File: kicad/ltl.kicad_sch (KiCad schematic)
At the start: 59 parts, among them J1 Conn_01x06, Q1 RUM001L02T2CL, Q2 RZM001P02T2L, Q3 BC327, U1 TPL5111, U2 ESP-12E, U3 DS18B20, U4 TPS73733DCQR

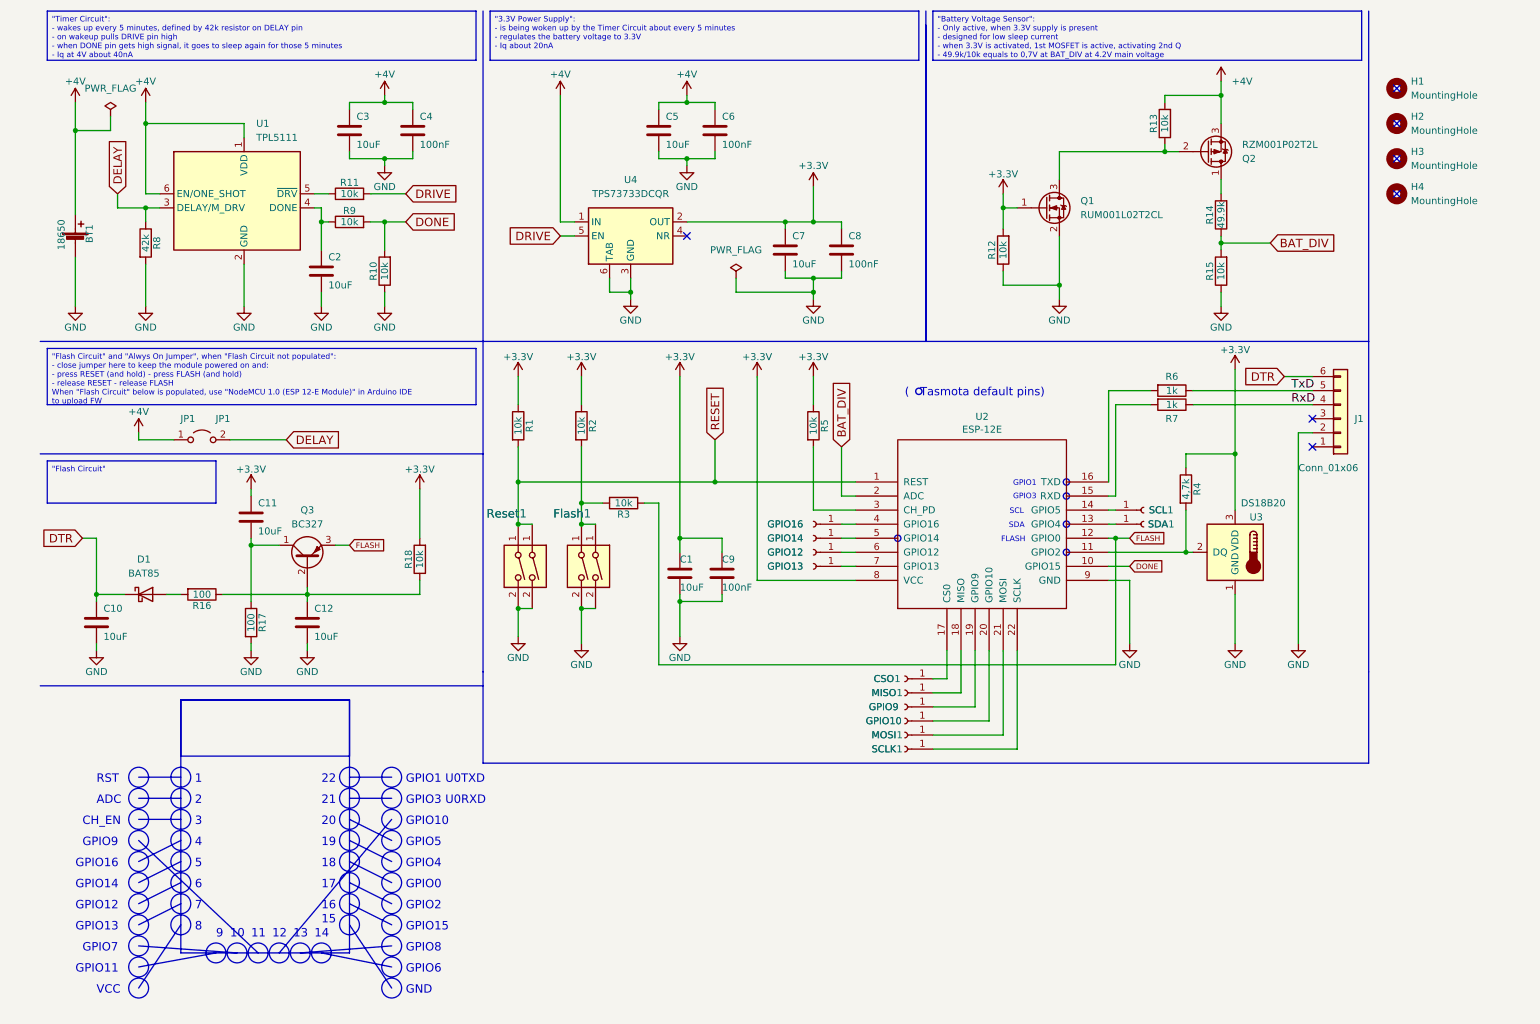
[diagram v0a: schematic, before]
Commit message: Updated PCB to Revision 2.2
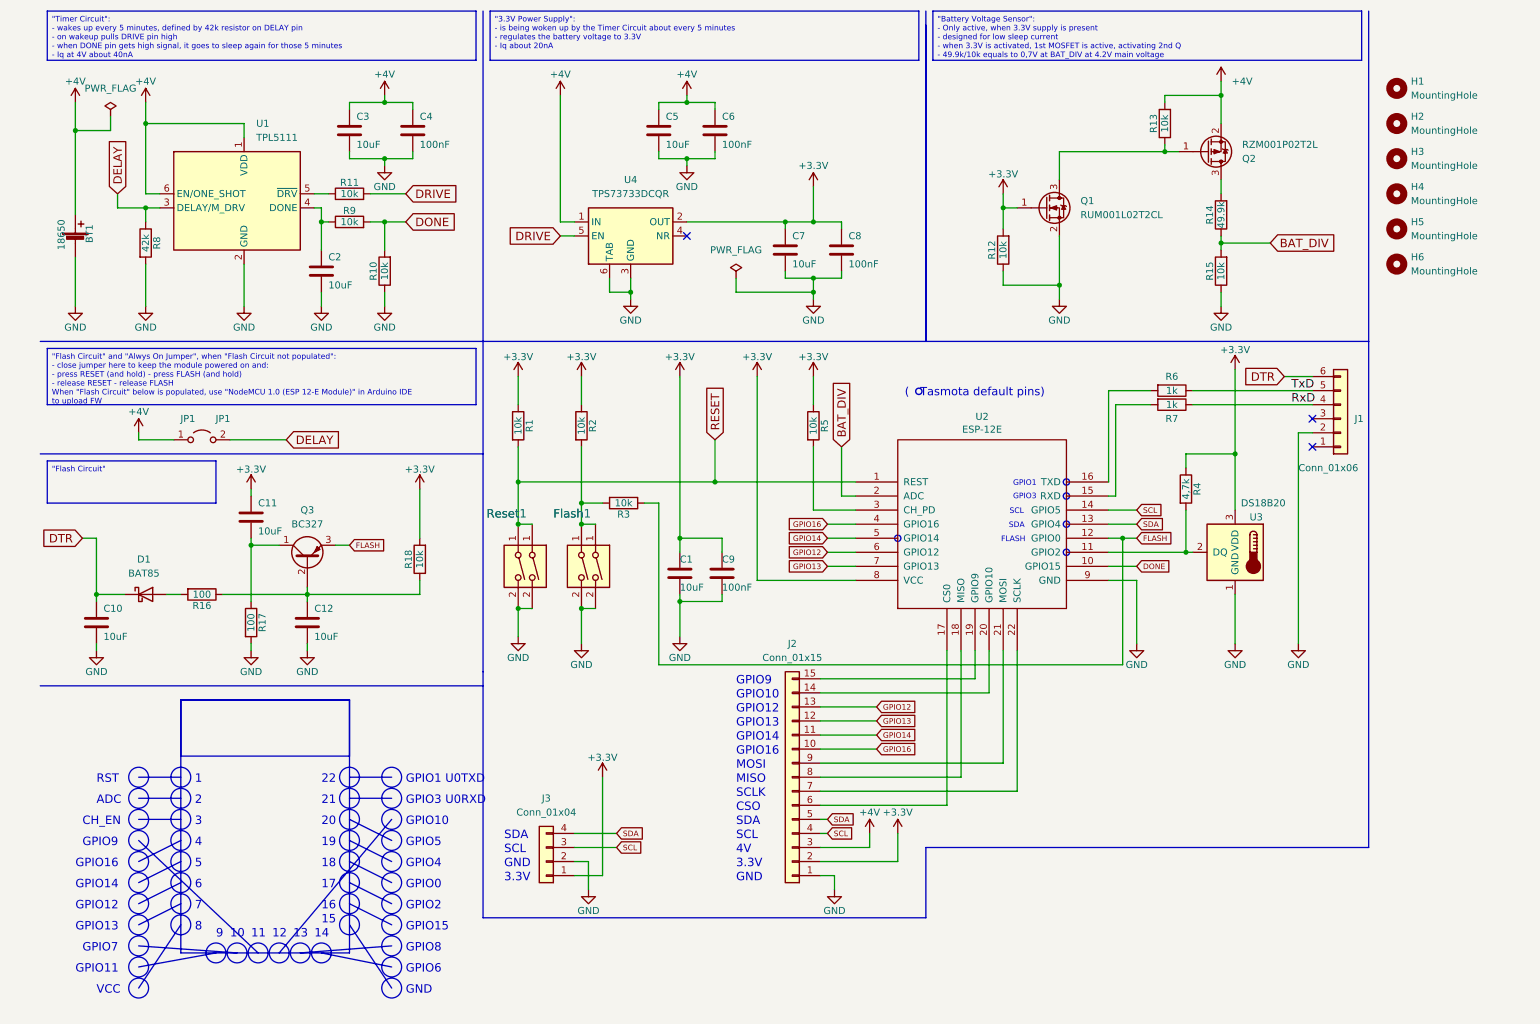
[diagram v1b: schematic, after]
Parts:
- removed CSO1: CSO, Connector_PinHeader_2.54mm:PinHeader_1x01_P2.54mm_Vertical, symbol Connector:Conn_01x01_Socket
- removed GPIO10: GPIO10, Connector_PinHeader_2.54mm:PinHeader_1x01_P2.54mm_Vertical, symbol Connector:Conn_01x01_Socket
- removed GPIO12: GPIO12, Connector_PinHeader_2.54mm:PinHeader_1x01_P2.54mm_Vertical, symbol Connector:Conn_01x01_Socket
- removed GPIO13: GPIO13, Connector_PinHeader_2.54mm:PinHeader_1x01_P2.54mm_Vertical, symbol Connector:Conn_01x01_Socket
- removed GPIO14: GPIO14, Connector_PinHeader_2.54mm:PinHeader_1x01_P2.54mm_Vertical, symbol Connector:Conn_01x01_Socket
- removed GPIO16: GPIO16, Connector_PinHeader_2.54mm:PinHeader_1x01_P2.54mm_Vertical, symbol Connector:Conn_01x01_Socket
- removed GPIO9: GPIO9, Connector_PinHeader_2.54mm:PinHeader_1x01_P2.54mm_Vertical, symbol Connector:Conn_01x01_Socket
- removed MISO1: MISO, Connector_PinHeader_2.54mm:PinHeader_1x01_P2.54mm_Vertical, symbol Connector:Conn_01x01_Socket
- removed MOSI1: MOSI, Connector_PinHeader_2.54mm:PinHeader_1x01_P2.54mm_Vertical, symbol Connector:Conn_01x01_Socket
- removed SCL1: SCL, Connector_PinHeader_2.54mm:PinHeader_1x01_P2.54mm_Vertical, symbol Connector:Conn_01x01_Socket
- removed SCLK1: SCLK, Connector_PinHeader_2.54mm:PinHeader_1x01_P2.54mm_Vertical, symbol Connector:Conn_01x01_Socket
- removed SDA1: SDA, Connector_PinHeader_2.54mm:PinHeader_1x01_P2.54mm_Vertical, symbol Connector:Conn_01x01_Socket
- added H5, H6: MountingHole, MountingHole:MountingHole_3.2mm_M3_Pad_Via, symbol Mechanical:MountingHole
- added J2: Conn_01x15, Connector_PinHeader_2.54mm:PinHeader_1x15_P2.54mm_Vertical, symbol Connector_Generic:Conn_01x15
- added J3: Conn_01x04, Connector_PinHeader_2.54mm:PinHeader_1x04_P2.54mm_Vertical, symbol Connector_Generic:Conn_01x04
- C11, C12: footprint Capacitor_THT:CP_Radial_D5.0mm_P2.00mm -> Capacitor_SMD:C_1206_3216Metric
- J1: footprint Connector_PinHeader_2.54mm:PinHeader_1x06_P2.54mm_Horizontal -> Connector_PinHeader_2.54mm:PinHeader_1x06_P2.54mm_Vertical
- R1, R10, R11, R12, R13, R14, R15, R16, R17, R18, R2, R3, R4, R5, R6, R7, R8, R9: footprint Resistor_THT:R_Axial_DIN0411_L9.9mm_D3.6mm_P12.70mm_Horizontal -> Resistor_THT:R_Axial_DIN0207_L6.3mm_D2.5mm_P10.16mm_Horizontal
- U2: footprint RF_Module:ESP-12E -> ESP8266MOD:ESP8266MOD
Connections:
- net +3V3: now also J2.2 (Pin_2), J3.1 (Pin_1)
- net +4V: now also Q2.2 (S), J2.3 (Pin_3); no longer Q2.3 (S)
- net GND: now also J2.1 (Pin_1), J3.2 (Pin_2)
- net SDA: now reaches U2.13 (GPIO4)
- net SDA: now also J2.5 (Pin_5), J3.4 (Pin_4)
- net SCL: now reaches U2.14 (GPIO5)
- net SCL: now also J2.4 (Pin_4), J3.3 (Pin_3)
- net at U2.17 (CS0): now also J2.6 (Pin_6)
- net at U2.18 (MISO): now also J2.8 (Pin_8)
- net at U2.19 (GPIO9): now also J2.15 (Pin_15)
- net at U2.20 (GPIO10): now also J2.14 (Pin_14)
- net at U2.21 (MOSI): now also J2.9 (Pin_9)
- net at U2.22 (SCLK): now also J2.7 (Pin_7)
- net GPIO16: now reaches U2.4 (GPIO16)
- net GPIO16: now also J2.10 (Pin_10)
- net GPIO14: now reaches U2.5 (GPIO14)
- net GPIO14: now also J2.11 (Pin_11)
- net GPIO12: now reaches U2.6 (GPIO12)
- net GPIO12: now also J2.13 (Pin_13)
- net GPIO13: now reaches U2.7 (GPIO13)
- net GPIO13: now also J2.12 (Pin_12)
- net at Q2.1 (G): now also Q1.3 (D), R13.1; no longer R14.2
- new net: Q2.3 (D), R14.2
- no-connect marks 7 -> 3
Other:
- note added: "3.3V"
- note added: "4V"
- note added: "CSO"
- note added: "MISO"
- note added: "MOSI"
- note added: "SCLK"

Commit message: Updated Readme
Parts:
- removed BT1: 18650, 18650:18650_small, symbol ltl-rescue:Battery_Cell
- removed H1, H2, H3, H4, H5, H6: MountingHole, MountingHole:MountingHole_3.2mm_M3_Pad_Via, symbol Mechanical:MountingHole
- added BT1: 1042, keystone_18650:BAT_1042, symbol keystone_18650:1042
- added D2: LED Green, LED_THT:LED_D3.0mm_Clear, symbol Device:LED
- added D3: LED Red, LED_THT:LED_D3.0mm_Clear, symbol Device:LED
- added H1, H2, H3, H4, H5, H6: MountingHole_Pad, MountingHole:MountingHole_3.2mm_M3_Pad_Via, symbol Mechanical:MountingHole_Pad
- added J1: Charger, Connector_PinHeader_2.54mm:PinHeader_1x03_P2.54mm_Vertical, symbol Connector_Generic:Conn_01x03
- added R17, R20: 2k, Resistor_THT:R_Axial_DIN0207_L6.3mm_D2.5mm_P10.16mm_Horizontal, symbol ltl-rescue:R
- added TP1: Done, TestPoint:TestPoint_Loop_D1.80mm_Drill1.0mm_Beaded, symbol Connector:TestPoint
- added TP2: Drive, TestPoint:TestPoint_Loop_D1.80mm_Drill1.0mm_Beaded, symbol Connector:TestPoint
- added TP3: BatDiv, TestPoint:TestPoint_Loop_D1.80mm_Drill1.0mm_Beaded, symbol Connector:TestPoint
- added TP4: Flash, TestPoint:TestPoint_Loop_D1.80mm_Drill1.0mm_Beaded, symbol Connector:TestPoint
- added TP5: Reset, TestPoint:TestPoint_Loop_D1.80mm_Drill1.0mm_Beaded, symbol Connector:TestPoint
- C8: renamed from C1; value 10uF -> 100uF
- Q1: renamed from Q3; footprint Package_TO_SOT_THT:TO-92_Inline -> Package_TO_SOT_THT:TO-92_Inline_Wide
- R18: renamed from R14; value 49.9k -> 39K
- U1: value TPL5111 -> TPL5111DDCR
- renumbered C10 to C1, C9 to C10, C7 to C11, C8 to C12, C11 to C2, C12 to C3, C2 to C4, C3 to C5, C4 to C6, C5 to C7, C6 to C9, J3 to J2, J2 to J3, J1 to J4, Q1 to Q2, Q2 to Q3, R8 to R1, R3 to R10, R5 to R11, R6 to R14, R7 to R15, R4 to R16, R15 to R19, R16 to R2, R17 to R3, R11 to R4, R9 to R5, R10 to R6, R18 to R7, R1 to R8, R2 to R9, U4 to U2, U2 to U3, U3 to U4
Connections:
- net +3V3: now also R17.1
- net +4V: now also J1.3 (Pin_3), R20.1
- net BAT_DIV: now also TP3.1
- net DONE: now also TP1.1
- net DRIVE: now also TP2.1
- net FLASH: now also TP4.1
- net GND: now also J4.1 (Pin_1), BT1.N, D2.1 (K), D3.1 (K), H1.1, H2.1, H3.1, H4.1, H5.1, H6.1, J1.1 (Pin_1); no longer C1.2, J4.2 (Pin_2)
- net GPIO12: now also R16.2, U4.2 (DQ); no longer J3.13 (Pin_13)
- net RESET: now also C1.2, TP5.1
- new net: D3.2 (A), R20.2
- new net: BT1.P, J1.2 (Pin_2)
- new net: D2.2 (A), R17.2
- new net GPIO2: J3.13 (Pin_13), U3.11 (GPIO2)
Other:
- moved on the sheet: C1, C4, C5, C6, R1, R4, R5, R6, U1

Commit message: A couple of addictions
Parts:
- removed D2: LED Green, LED_THT:LED_D3.0mm_Clear, symbol Device:LED
- removed D3: LED Red, LED_THT:LED_D3.0mm_Clear, symbol Device:LED
- removed J1: Charger, Connector_PinHeader_2.54mm:PinHeader_1x03_P2.54mm_Vertical, symbol Connector_Generic:Conn_01x03
- removed J3: Conn_01x15, Connector_PinHeader_2.54mm:PinHeader_1x15_P2.54mm_Vertical, symbol Connector_Generic:Conn_01x15
- removed R17, R20: 2k, Resistor_THT:R_Axial_DIN0207_L6.3mm_D2.5mm_P10.16mm_Horizontal, symbol ltl-rescue:R
- added F1: Fuse_Small, Fuse:Fuse_1206_3216Metric_Pad1.42x1.75mm_HandSolder, symbol Device:Fuse_Small
- added J1: Conn_01x04, Connector_PinHeader_2.54mm:PinHeader_1x04_P2.54mm_Vertical, symbol Connector_Generic:Conn_01x04
- added J3: Conn_01x16, Connector_PinHeader_2.54mm:PinHeader_1x16_P2.54mm_Vertical, symbol Connector_Generic:Conn_01x16
- R1: value 42k -> 43K
- R10, R11, R12, R13, R4, R5, R6, R7, R8, R9: value 10k -> 10K
- R14, R15: value 1k -> 1K
- R16: value 4,7k -> 4.7K
- R18: renamed from R19; value 10k -> 10K
- renumbered R18 to R17
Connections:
- net +3V3: now also J3.3 (Pin_3)
- net +4V: now also F1.2, J1.4 (Pin_4), J3.4 (Pin_4)
- net GND: now also J1.1 (Pin_1), J3.1 (Pin_1); no longer BT1.N
- net GPIO13: now also J3.13 (Pin_13)
- net GPIO14: now also J3.12 (Pin_12)
- net GPIO16: now also J3.11 (Pin_11)
- net GPIO2: now also J3.16 (Pin_16)
- net SCL: now also J3.5 (Pin_5)
- net SDA: now also J3.6 (Pin_6)
- net at U3.17 (CS0): now also J3.7 (Pin_7)
- net at U3.18 (MISO): now also J3.9 (Pin_9)
- net at U3.19 (GPIO9): now also J3.15 (Pin_15)
- net at U3.20 (GPIO10): now also J3.14 (Pin_14)
- net at U3.21 (MOSI): now also J3.10 (Pin_10)
- net at U3.22 (SCLK): now also J3.8 (Pin_8)
- net at BT1.P: now also F1.1
- new net: BT1.N, J1.2 (Pin_2)
- no-connect marks 3 -> 5
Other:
- note removed: "1"
- note removed: "10"
- note removed: "11"
- note removed: "12"
- note removed: "13"
- note removed: "14"
- note removed: "15"
- note removed: "16"
- note removed: "17"
- note removed: "18"
- note removed: "19"
- note removed: "2"
- note removed: "20"
- note removed: "21"
- note removed: "22"
- note removed: "3"
- note removed: "4"
- note removed: "5"
- note removed: "6"
- note removed: "7"
- note removed: "8"
- note removed: "9"
- note removed: "ADC"
- note removed: "CH_EN"
- note removed: "GPIO0"
- note removed: "GPIO1 U0TXD"
- note removed: "GPIO11"
- note removed: "GPIO12"
- note removed: "GPIO15"
- note removed: "GPIO3 U0RXD"
- note removed: "GPIO4"
- note removed: "GPIO5"
- note removed: "GPIO6"
- note removed: "GPIO7"
- note removed: "GPIO8"
- note removed: "RST"
- note removed: "VCC"
- moved on the sheet: BT1, JP1

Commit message: Updated last image
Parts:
- BT1: footprint keystone_18650:BAT_1042 -> 18650:18650_flat
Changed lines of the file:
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@@
   )
   (text_box "5m"
-    (at 26.035 156.21 0) (size 19.05 3.81)
+    (at 26.035 156.21 0) (size 21.59 3.81)
     (stroke (width 0) (type default))
     (fill (type none))
@@
   )
   (text_box "42.887K"
-    (at 45.085 156.21 0) (size 19.05 3.81)
+    (at 46.99 182.245 0) (size 17.78 3.81)
+    (stroke (width 0) (type default))
+    (fill (type none))
+    (effects (font (size 1.524 1.524) (thickness 0.3048) bold) (justify top))
+  )
+  (text_box "5V"
+    (at 64.77 174.625 0) (size 17.78 3.81)
+    (stroke (width 0) (type default))
+    (fill (type none))
+    (effects (font (size 1.524 1.524) (thickness 0.3048) bold) (justify top))
+  )
+  (text_box "57.437K"
+    (at 46.99 186.055 0) (size 17.78 3.81)
+    (stroke (width 0) (type default))
+    (fill (type none))
+    (effects (font (size 1.524 1.524) (thickness 0.3048) bold) (justify top))
+  )
+  (text_box "92.23K"
+    (at 64.77 189.865 0) (size 17.78 3.81)
+    (stroke (width 0) (type default))
+    (fill (type none))
+    (effects (font (size 1.524 1.524) (thickness 0.3048) bold) (justify top))
+  )
+  (text_box "42.887K"
+    (at 47.625 156.21 0) (size 25.4 3.81)
     (stroke (width 0) (type default))
     (fill (type none))
@@
     (effects (font (face "KiCad Font") (size 1 1)) (justify left top))
   )
+  (text_box "29.349K"
+    (at 64.77 178.435 0) (size 17.78 3.81)
+    (stroke (width 0) (type default))
+    (fill (type none))
+    (effects (font (size 1.524 1.524) (thickness 0.3048) bold) (justify top))
+  )
   (text_box "57.437K"
-    (at 45.085 160.02 0) (size 19.05 3.81)
+    (at 47.625 160.02 0) (size 25.4 3.81)
     (stroke (width 0) (type default))
     (fill (type none))
@@
   )
   (text_box "2m"
-    (at 26.035 152.4 0) (size 19.05 3.81)
+    (at 26.035 152.4 0) (size 21.59 3.81)
+    (stroke (width 0) (type default))
+    (fill (type none))
+    (effects (font (size 1.524 1.524) (thickness 0.3048) bold) (justify top))
+  )
+  (text_box "29.349K"
+    (at 46.99 178.435 0) (size 17.78 3.81)
     (stroke (width 0) (type default))
     (fill (type none))
@@
   )
   (text_box "1m"
-    (at 26.035 148.59 0) (size 19.05 3.81)
+    (at 26.035 148.59 0) (size 21.59 3.81)
+    (stroke (width 0) (type default))
+    (fill (type none))
+    (effects (font (size 1.524 1.524) (thickness 0.3048) bold) (justify top))
+  )
+  (text_box "Values for R17 and associated Voltage Levels"
+    (at 26.035 170.815 0) (size 56.515 3.81)
     (stroke (width 0) (type default))
     (fill (type none))
@@
   )
   (text_box "92.23K"
-    (at 45.085 163.83 0) (size 19.05 3.81)
+    (at 47.625 163.83 0) (size 25.4 3.81)
+    (stroke (width 0) (type default))
+    (fill (type none))
+    (effects (font (size 1.524 1.524) (thickness 0.3048) bold) (justify top))
+  )
+  (text_box "92.23K"
+    (at 46.99 189.865 0) (size 17.78 3.81)
+    (stroke (width 0) (type default))
+    (fill (type none))
+    (effects (font (size 1.524 1.524) (thickness 0.3048) bold) (justify top))
+  )
+  (text_box "Vcc"
+    (at 26.035 174.625 0) (size 20.955 3.81)
+    (stroke (width 0) (type default))
+    (fill (type none))
+    (effects (font (size 1.524 1.524) (thickness 0.3048) bold) (justify top))
+  )
+  (text_box "57.437K"
+    (at 64.77 186.055 0) (size 17.78 3.81)
     (stroke (width 0) (type default))
     (fill (type none))
@@
   )
   (text_box "10m"
-    (at 26.035 160.02 0) (size 19.05 3.81)
+    (at 26.035 160.02 0) (size 21.59 3.81)
+    (stroke (width 0) (type default))
+    (fill (type none))
+    (effects (font (size 1.524 1.524) (thickness 0.3048) bold) (justify top))
+  )
+  (text_box "2m"
+    (at 26.035 178.435 0) (size 20.955 3.81)
     (stroke (width 0) (type default))
     (fill (type none))
@@
     (effects (font (face "KiCad Font") (size 1 1)) (justify left top))
   )
+  (text_box "5m"
+    (at 26.035 182.245 0) (size 20.955 3.81)
+    (stroke (width 0) (type default))
+    (fill (type none))
+    (effects (font (size 1.524 1.524) (thickness 0.3048) bold) (justify top))
+  )
+  (text_box "4.2V"
+    (at 46.99 174.625 0) (size 17.78 3.81)
+    (stroke (width 0) (type default))
+    (fill (type none))
+    (effects (font (size 1.524 1.524) (thickness 0.3048) bold) (justify top))
+  )
   (text_box "22,02K"
-    (at 45.085 148.59 0) (size 19.05 3.81)
+    (at 47.625 148.59 0) (size 25.4 3.81)
+    (stroke (width 0) (type default))
+    (fill (type none))
+    (effects (font (size 1.524 1.524) (thickness 0.3048) bold) (justify top))
+  )
+  (text_box "10m"
+    (at 26.035 186.055 0) (size 20.955 3.81)
     (stroke (width 0) (type default))
     (fill (type none))
@@
     (effects (font (face "KiCad Font") (size 1 1)) (justify left top))
   )
+  (text_box "30m"
+    (at 26.035 189.865 0) (size 20.955 3.81)
+    (stroke (width 0) (type default))
+    (fill (type none))
+    (effects (font (size 1.524 1.524) (thickness 0.3048) bold) (justify top))
+  )
   (text_box "29.349K"
-    (at 45.085 152.4 0) (size 19.05 3.81)
+    (at 47.625 152.4 0) (size 25.4 3.81)
     (stroke (width 0) (type default))
     (fill (type none))
@@
   )
   (text_box "30m"
-    (at 26.035 163.83 0) (size 19.05 3.81)
+    (at 26.035 163.83 0) (size 21.59 3.81)
     (stroke (width 0) (type default))
     (fill (type none))
@@
     (effects (font (face "KiCad Font") (size 1 1)) (justify left top))
   )
-  (text_box "Values for R1 and Timings"
-    (at 26.035 144.78 0) (size 38.1 3.81)
+  (text_box "42.887K"
+    (at 64.77 182.245 0) (size 17.78 3.81)
+    (stroke (width 0) (type default))
+    (fill (type none))
+    (effects (font (size 1.524 1.524) (thickness 0.3048) bold) (justify top))
+  )
+  (text_box "Values for R1 and associated Timings"
+    (at 26.035 144.78 0) (size 46.99 3.81)
     (stroke (width 0) (type default))
     (fill (type none))
@@
       (effects (font (size 1.27 1.27)) (justify left))
     )
-    (property "Footprint" "keystone_18650:BAT_1042" (at 24.765 48.26 0)
+    (property "Footprint" "18650:18650_flat" (at 24.765 48.26 0)
       (effects (font (size 1.27 1.27)) (justify bottom) hide)
     )
